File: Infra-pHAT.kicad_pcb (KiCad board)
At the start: 2 copper layers, 65 x 30 mm, 26 parts, among them Q1 BC817, U1 CAT24C32WI-GT3

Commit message: completed layout
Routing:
- net Net-(R6-Pad2): track 45.8 -> 39.0 mm
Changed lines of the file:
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@@
     (thickness 1.6)
     (drawings 30)
-    (tracks 242)
+    (tracks 239)
     (zones 0)
     (modules 26)
@@
   (segment (start 175.514 91.567) (end 174.371 92.71) (width 0.5) (layer F.Cu) (net 10) (status 80000))
   (segment (start 174.371 92.71) (end 174.41 92.66) (width 0.5) (layer F.Cu) (net 10) (status 80000))
-  (segment (start 180.34 86.36) (end 180.34 88.9) (width 0.5) (layer F.Cu) (net 10))
-  (segment (start 180.34 88.9) (end 179.07 90.17) (width 0.5) (layer F.Cu) (net 10))
-  (segment (start 179.07 90.17) (end 179.07 96.52) (width 0.5) (layer F.Cu) (net 10))
-  (segment (start 179.07 96.52) (end 180.34 96.52) (width 0.5) (layer F.Cu) (net 10))
+  (segment (start 180.34 91.44) (end 180.34 86.36) (width 0.5) (layer F.Cu) (net 10))
   (segment (start 183.3 86.48) (end 183.261 86.487) (width 0.5) (layer F.Cu) (net 11) (status 80000))
   (segment (start 183.261 86.487) (end 182.245 85.471) (width 0.5) (layer F.Cu) (net 11) (status 80000))

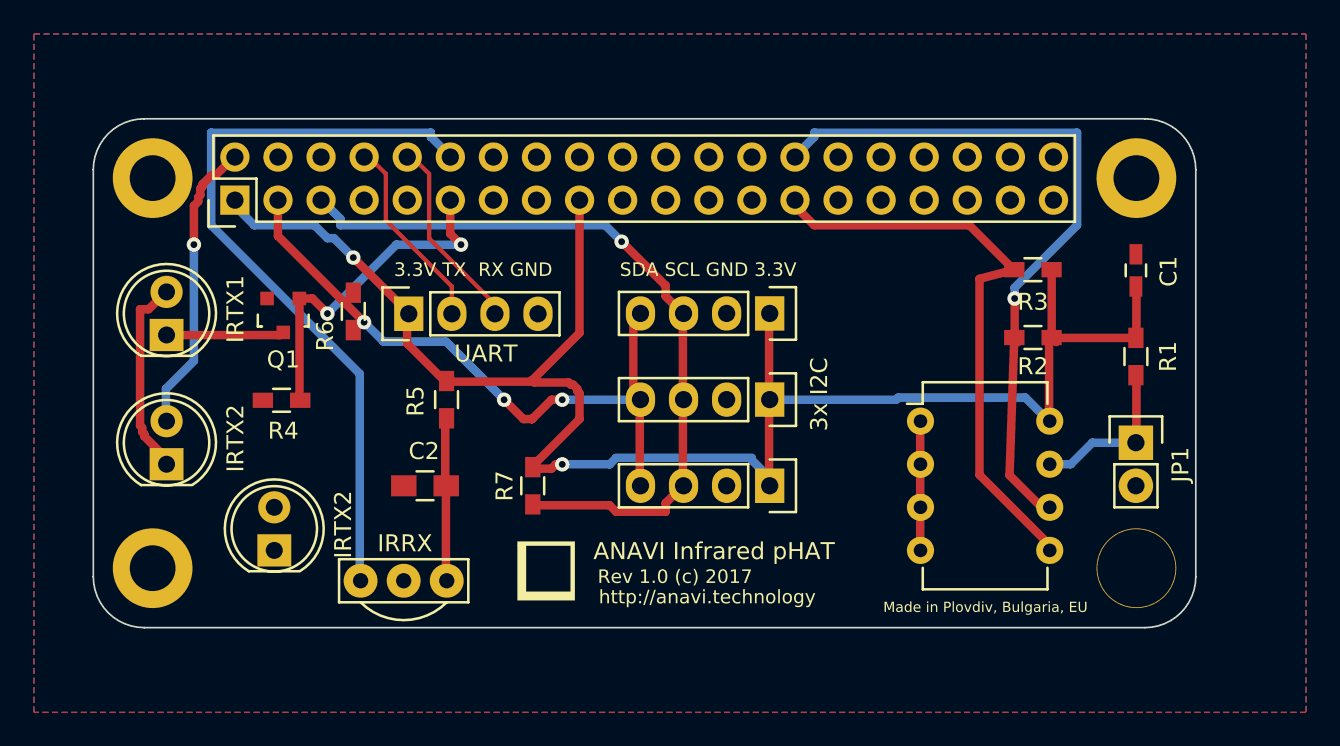
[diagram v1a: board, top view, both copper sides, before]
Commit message: adjusted 74HC81 position
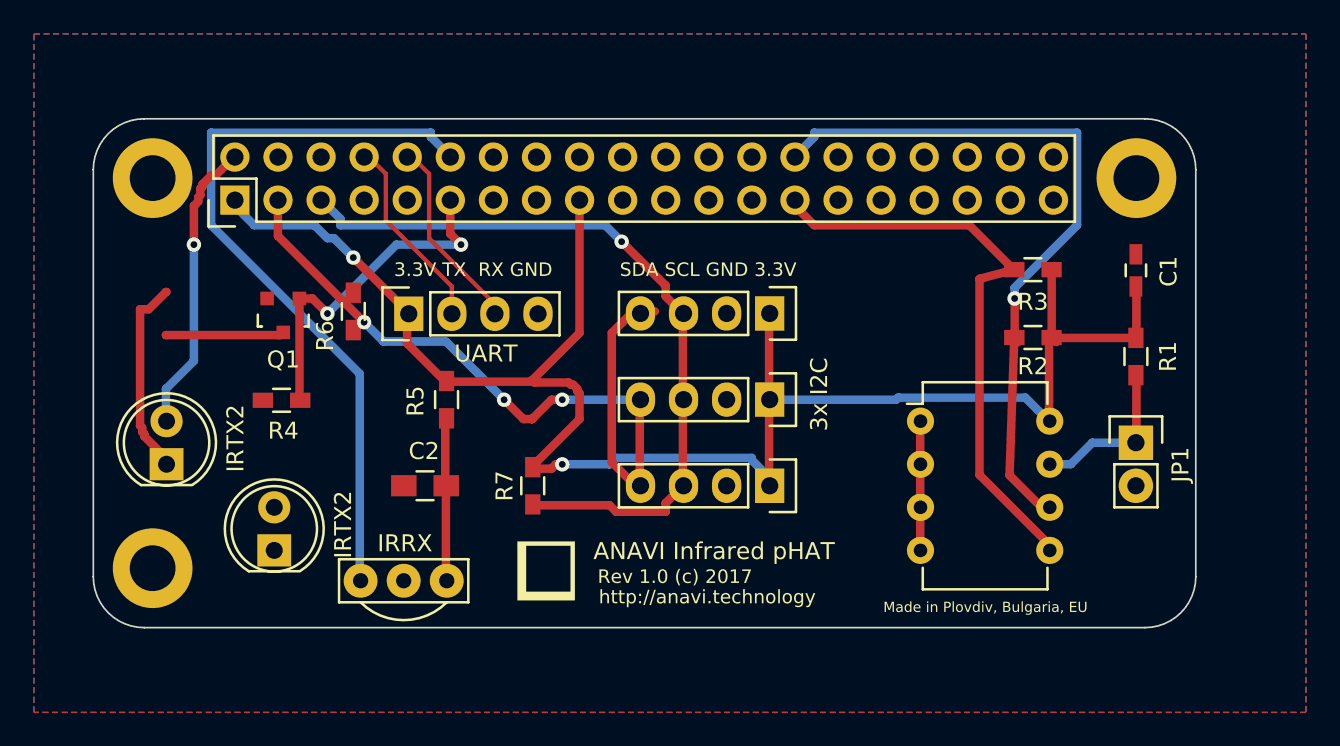
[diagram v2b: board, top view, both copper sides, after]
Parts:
- removed IRTX1: L-53F3BT, LEDs:LED-5MM
- removed REF3: MountingHole_2.7mm_M2.5_DIN965_Pad, Mounting_Holes:MountingHole_2.7mm_M2.5_DIN965_Pad
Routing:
- net Net-(R6-Pad2): track 39.0 -> 46.4 mm
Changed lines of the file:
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@@
     (thickness 1.6)
     (drawings 30)
-    (tracks 239)
+    (tracks 242)
     (zones 0)
-    (modules 26)
+    (modules 24)
     (nets 36)
   )
@@
   )
   (layers
-    (0 F.Cu signal)
-    (31 B.Cu signal)
+    (0 F.Cu signal hide)
+    (31 B.Cu signal hide)
     (32 B.Adhes user)
     (33 F.Adhes user)
@@
   )
   (module LEDs:LED-5MM (layer F.Cu)
-    (at 152.82 87.75 90)
-    (descr "LED 5mm round vertical")
-    (tags "LED 5mm round vertical")
-    (fp_text reference IRTX1 (at 1.524 4.064 90) (layer F.SilkS)
-      (effects (font (size 1 1) (thickness 0.15)))
-    )
-    (fp_text value L-53F3BT (at 1.524 -3.937 90) (layer F.Fab) hide
-      (effects (font (size 1 1) (thickness 0.15)))
-    )
-    (fp_line (start -1.5 -1.55) (end -1.5 1.55) (layer F.CrtYd) (width 0.05))
-    (fp_arc (start 1.3 0) (end -1.5 1.55) (angle -302) (layer F.CrtYd) (width 0.05))
-    (fp_arc (start 1.27 0) (end -1.23 -1.5) (angle 297.5) (layer F.SilkS) (width 0.15))
-    (fp_line (start -1.23 1.5) (end -1.23 -1.5) (layer F.SilkS) (width 0.15))
-    (fp_circle (center 1.27 0) (end 0.97 -2.5) (layer F.SilkS) (width 0.15))
-    (fp_text user K (at -1.905 1.905 90) (layer F.SilkS) hide
-      (effects (font (size 1 1) (thickness 0.15)))
-    )
-    (pad 1 thru_hole rect (at 0 0 180) (size 2 1.9) (drill 1.00076) (layers *.Cu *.Mask F.SilkS)
-      (net 15 "Net-(IRTX1-Pad1)"))
-    (pad 2 thru_hole circle (at 2.54 0 90) (size 1.9 1.9) (drill 1.00076) (layers *.Cu *.Mask F.SilkS)
-      (net 4 "Net-(IRTX1-Pad2)"))
-    (model LEDs.3dshapes/LED-5MM.wrl
-      (offset (xyz 1.269999980926514 0 0))
-      (scale (xyz 1 1 1))
-      (rotate (xyz 0 0 90))
-    )
-  )
-  (module LEDs:LED-5MM (layer F.Cu)
     (at 152.82 95.37 90)
     (descr "LED 5mm round vertical")
@@
     (fp_circle (center 0 0) (end 2.6 0) (layer F.CrtYd) (width 0.05))
     (pad 2 thru_hole circle (at 0 0) (size 4.7 4.7) (drill 2.7) (layers *.Cu *.Mask F.SilkS))
-  )
-  (module Mounting_Holes:MountingHole_2.7mm_M2.5_DIN965_Pad (layer F.Cu)
-    (at 210 101.5)
-    (descr "Mounting Hole 2.7mm, M2.5, DIN965")
-    (tags "mounting hole 2.7mm m2.5 din965")
-    (fp_text reference REF3 (at 0 -3.35) (layer F.SilkS) hide
-      (effects (font (size 1 1) (thickness 0.15)))
-    )
-    (fp_text value MountingHole_2.7mm_M2.5_DIN965_Pad (at 0 3.35) (layer F.Fab) hide
-      (effects (font (size 1 1) (thickness 0.15)))
-    )
-    (fp_circle (center 0 0) (end 2.35 0) (layer Cmts.User) (width 0.15))
-    (fp_circle (center 0 0) (end 2.6 0) (layer F.CrtYd) (width 0.05))
-    (pad 3 thru_hole circle (at 0 0) (size 4.7 4.7) (drill 4.6) (layers *.Cu *.Mask F.SilkS))
   )
   (module Mounting_Holes:MountingHole_2.7mm_M2.5_DIN965_Pad (layer F.Cu)
@@
   (segment (start 175.514 91.567) (end 174.371 92.71) (width 0.5) (layer F.Cu) (net 10) (status 80000))
   (segment (start 174.371 92.71) (end 174.41 92.66) (width 0.5) (layer F.Cu) (net 10) (status 80000))
-  (segment (start 180.34 91.44) (end 180.34 86.36) (width 0.5) (layer F.Cu) (net 10))
+  (segment (start 181.61 86.36) (end 180.34 86.36) (width 0.5) (layer F.Cu) (net 10))
+  (segment (start 180.34 86.36) (end 179.07 87.63) (width 0.5) (layer F.Cu) (net 10))
+  (segment (start 179.07 87.63) (end 179.07 95.25) (width 0.5) (layer F.Cu) (net 10))
+  (segment (start 179.07 95.25) (end 180.34 96.52) (width 0.5) (layer F.Cu) (net 10))
   (segment (start 183.3 86.48) (end 183.261 86.487) (width 0.5) (layer F.Cu) (net 11) (status 80000))
   (segment (start 183.261 86.487) (end 182.245 85.471) (width 0.5) (layer F.Cu) (net 11) (status 80000))

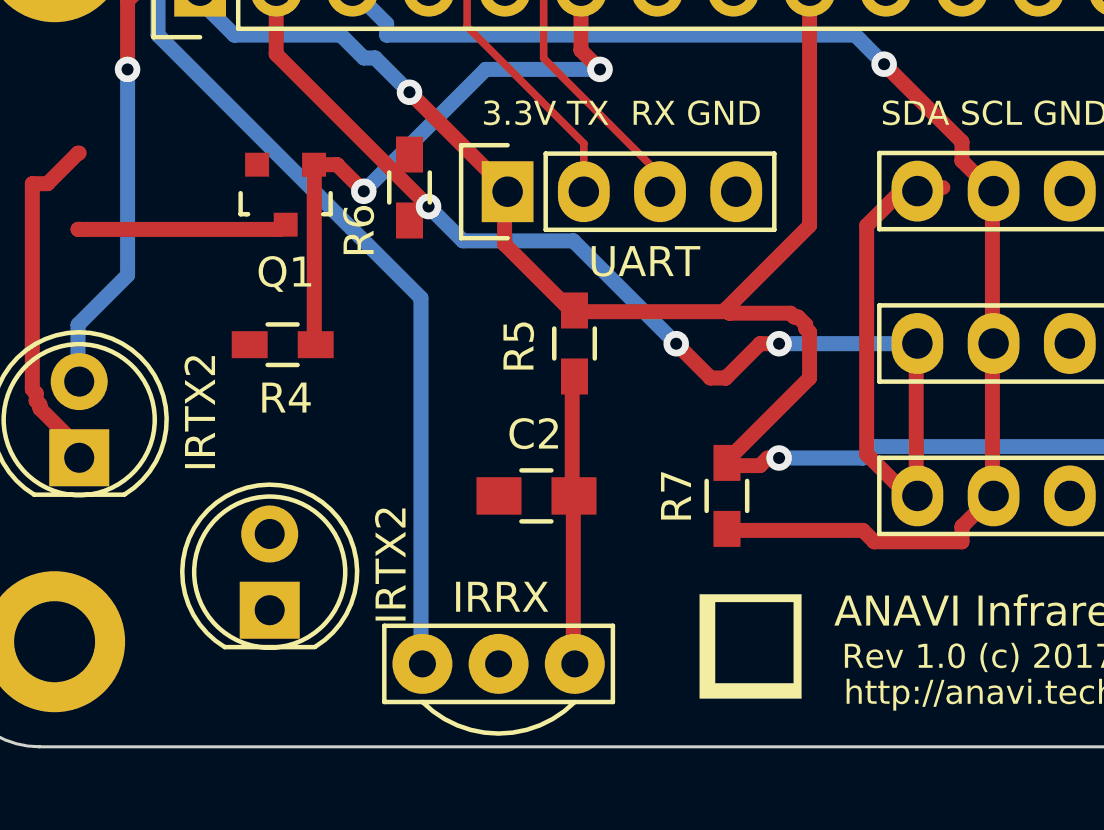
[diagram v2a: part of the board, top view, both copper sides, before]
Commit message: rerouted R6 Pad2 & deleted the Cap3
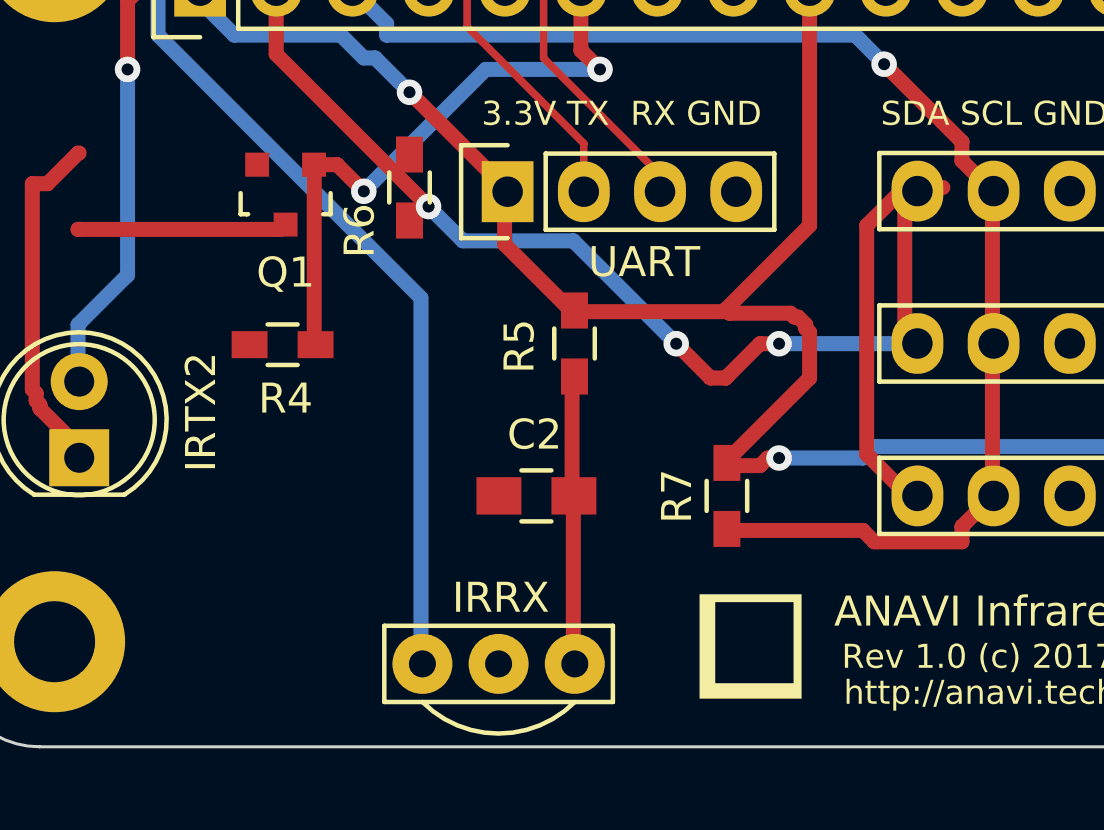
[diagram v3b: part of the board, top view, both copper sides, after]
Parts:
- removed the IRTX2 at (159.2, 100.5)
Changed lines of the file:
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@@
     (tracks 242)
     (zones 0)
-    (modules 24)
+    (modules 23)
     (nets 36)
   )
@@
     (uvia_dia 0.35)
     (uvia_drill 0.1)
-  )
-  (module LEDs:LED-5MM (layer F.Cu)
-    (at 159.17 100.45 90)
-    (descr "LED 5mm round vertical")
-    (tags "LED 5mm round vertical")
-    (fp_text reference IRTX2 (at 1.524 4.064 90) (layer F.SilkS)
-      (effects (font (size 1 1) (thickness 0.15)))
-    )
-    (fp_text value L-53F3BT (at 1.524 -3.937 90) (layer F.Fab) hide
-      (effects (font (size 1 1) (thickness 0.15)))
-    )
-    (fp_text user K (at -1.905 1.905 90) (layer F.SilkS) hide
-      (effects (font (size 1 1) (thickness 0.15)))
-    )
-    (fp_circle (center 1.27 0) (end 0.97 -2.5) (layer F.SilkS) (width 0.15))
-    (fp_line (start -1.23 1.5) (end -1.23 -1.5) (layer F.SilkS) (width 0.15))
-    (fp_arc (start 1.27 0) (end -1.23 -1.5) (angle 297.5) (layer F.SilkS) (width 0.15))
-    (fp_arc (start 1.3 0) (end -1.5 1.55) (angle -302) (layer F.CrtYd) (width 0.05))
-    (fp_line (start -1.5 -1.55) (end -1.5 1.55) (layer F.CrtYd) (width 0.05))
-    (pad 2 thru_hole circle (at 2.54 0 90) (size 1.9 1.9) (drill 1.00076) (layers *.Cu *.Mask F.SilkS))
-    (pad 1 thru_hole rect (at 0 0 180) (size 2 1.9) (drill 1.00076) (layers *.Cu *.Mask F.SilkS))
-    (model LEDs.3dshapes/LED-5MM.wrl
-      (offset (xyz 1.269999980926514 0 0))
-      (scale (xyz 1 1 1))
-      (rotate (xyz 0 0 90))
-    )
   )
   (module Capacitors_SMD:C_0603_HandSoldering (layer F.Cu)
@@
   (segment (start 180.721 91.567) (end 180.76 91.56) (width 0.5) (layer F.Cu) (net 10) (status 80000))
   (segment (start 180.76 91.56) (end 180.721 91.567) (width 0.5) (layer F.Cu) (net 10) (status 80000))
-  (segment (start 180.721 91.567) (end 180.721 96.647) (width 0.5) (layer F.Cu) (net 10) (status 80000))
   (segment (start 180.721 96.647) (end 180.76 96.64) (width 0.5) (layer F.Cu) (net 10) (status 80000))
   (segment (start 174.41 92.66) (end 174.371 92.71) (width 0.5) (layer F.Cu) (net 10) (status 80000))
@@
   (segment (start 181.61 86.36) (end 180.34 86.36) (width 0.5) (layer F.Cu) (net 10))
   (segment (start 180.34 86.36) (end 179.07 87.63) (width 0.5) (layer F.Cu) (net 10))
+  (segment (start 179.07 95.25) (end 180.34 96.52) (width 0.5) (layer F.Cu) (net 10))
   (segment (start 179.07 87.63) (end 179.07 95.25) (width 0.5) (layer F.Cu) (net 10))
-  (segment (start 179.07 95.25) (end 180.34 96.52) (width 0.5) (layer F.Cu) (net 10))
+  (segment (start 180.34 86.36) (end 180.34 91.44) (width 0.5) (layer F.Cu) (net 10))
   (segment (start 183.3 86.48) (end 183.261 86.487) (width 0.5) (layer F.Cu) (net 11) (status 80000))
   (segment (start 183.261 86.487) (end 182.245 85.471) (width 0.5) (layer F.Cu) (net 11) (status 80000))
